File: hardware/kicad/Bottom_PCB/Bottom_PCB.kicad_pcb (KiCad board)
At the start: 4 copper layers, 30.8 x 26.8 mm, 45 parts, among them Q7 IAUC60N04S6N031H, Q8 IAUC60N04S6N031H, Q9 IAUC60N04S6N031H, U5 STSPIN32F0ATR

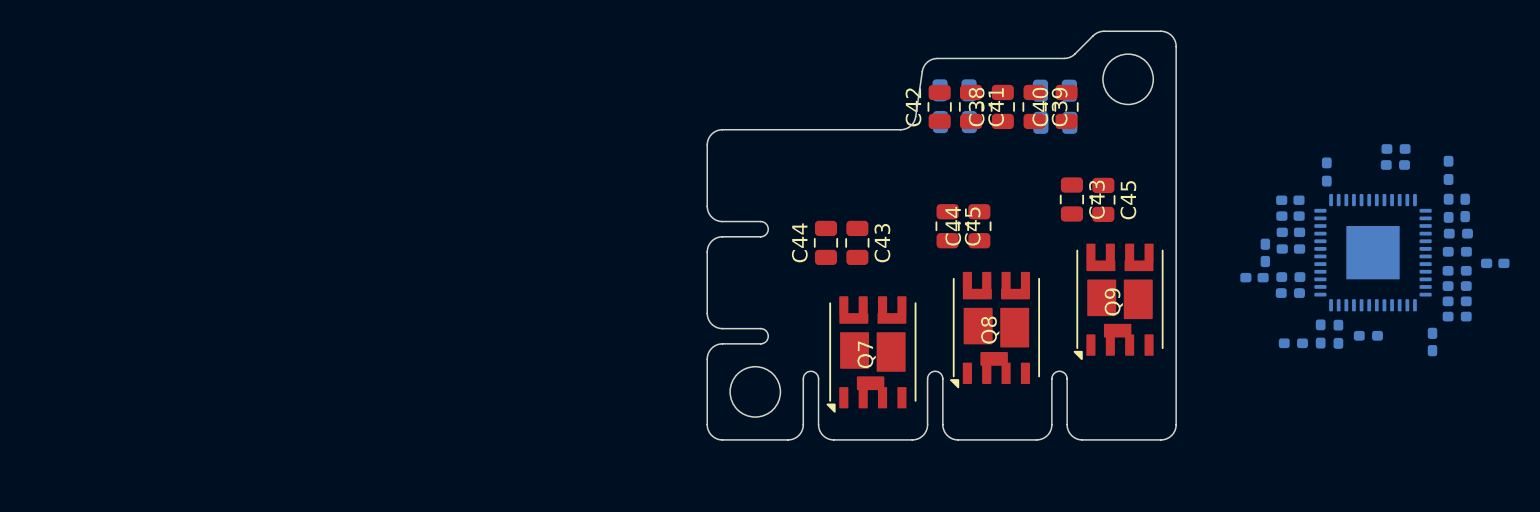
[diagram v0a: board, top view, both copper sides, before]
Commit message: Bottom PCB Design Checked and should be ready for review
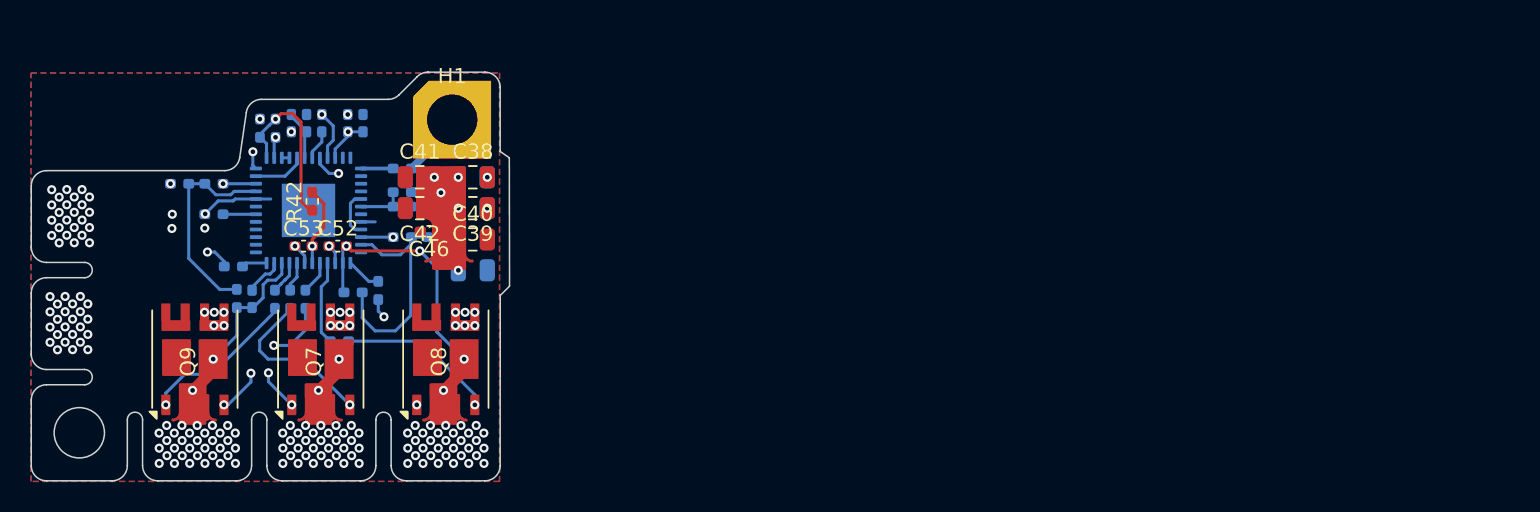
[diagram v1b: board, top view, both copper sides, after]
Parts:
- removed the C39 at (201.8, 88.2)
- removed the C39 at (203.1, 87.1)
- removed the C40 at (203.9, 88.2)
- removed the C40 at (203.1, 89.2)
- removed the C41 at (197.6, 88.2)
- removed the C41 at (196.5, 87.1)
- removed the C42 at (195.5, 88.2)
- removed the C42 at (196.5, 89.2)
- removed the C43 at (204.2, 94.2)
- removed the C43 at (190.1, 97.1)
- removed the C44 at (198.1, 96.0)
- removed the C44 at (188.1, 97.1)
- removed the C45 at (196.1, 96.0)
- removed the C45 at (206.3, 94.3)
- added C39: GRM21BR61A476ME15L, Capacitor_SMD:C_0805_2012Metric, F.Cu at (164.9, 94.8)
- added C40: GRM21BR61A476ME15L, Capacitor_SMD:C_0805_2012Metric, F.Cu at (164.9, 96.8)
- added C41: GRM21BR61A476ME15L, Capacitor_SMD:C_0805_2012Metric, F.Cu at (161.4, 92.8)
- added C42: GRM21BR61A476ME15L, Capacitor_SMD:C_0805_2012Metric, F.Cu at (161.4, 94.8)
- added C43: GRM21BR61A476ME15L, Capacitor_SMD:C_0805_2012Metric, B.Cu at (164.9, 94.8)
- added C44: GRM21BR61A476ME15L, Capacitor_SMD:C_0805_2012Metric, B.Cu at (164.9, 92.8)
- added C45: GRM21BR61A476ME15L, Capacitor_SMD:C_0805_2012Metric, B.Cu at (164.9, 98.9)
- added H1: PWM_Input, MountingHole:MountingHole_2.2mm_M2_DIN965_Pad_TopBottom, F.Cu at (163.6, 89.0)
- added R3: 100k, Resistor_SMD:R_0402_1005Metric_Pad0.72x0.64mm_HandSolder, B.Cu at (160.3, 93.8)
- added R4: 10k, Resistor_SMD:R_0402_1005Metric_Pad0.72x0.64mm_HandSolder, B.Cu at (160.3, 94.7)
- C46, C52, C53, R42: moved to F.Cu
- Q7, Q8, Q9: value IAUC60N04S6N031H -> IAUC60N04S6L045H
- moved R55 80.3 mm to (149.2, 98.6), turned to 180 degrees
- moved C53 78.2 mm to (153.8, 97.3)
- moved R54 77.5 mm to (151.9, 100.8), turned to -90 degrees
- moved C54 77.5 mm to (150.4, 100.8), turned to -90 degrees
- moved R52 76.5 mm to (152.9, 100.8), turned to -90 degrees
- moved R49 76.1 mm to (147.9, 95.2)
- moved R51 75.6 mm to (153.9, 100.8), turned to -90 degrees
- moved R42 75.2 mm to (154.4, 94.3), turned to 90 degrees
- moved C52 74.0 mm to (156.1, 97.3), turned to 0 degrees
- moved R41 73.8 mm to (145.7, 93.2)
- moved R50 73.7 mm to (156.2, 103.5)
- moved R40 73.2 mm to (147.9, 93.2), turned to 180 degrees
- moved R39 72.3 mm to (149.4, 100.7)
- moved R45 72.1 mm to (157.1, 100.3), turned to 0 degrees
- moved R53 70.6 mm to (158.7, 100.2), turned to -90 degrees
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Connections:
- R48 pad 1: /WPWM -> /PWM_INPUT
- U5 pad 18: /VSENSE -> Net-(U5-PA7)
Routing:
- net /BEMF_COMMON: track 0.00 -> 23.9 mm, vias 0 -> 3
- net /PHASE3: track 0.00 -> 16.4 mm, vias 0 -> 37
- net /BEMF3: track 0.00 -> 16.1 mm
- net Net-(Q9-LOW_GATE): track 0.00 -> 15.1 mm, vias 0 -> 3
- net +BATT: track 0.00 -> 13.7 mm, vias 0 -> 30
- net /BEMF1: track 0.00 -> 13.7 mm
- net /PHASE2: track 0.00 -> 13.4 mm, vias 0 -> 36
- net GND: track 0.00 -> 12.2 mm, vias 0 -> 52
- net /BEMF2: track 0.00 -> 11.4 mm, vias 0 -> 1
- net +3.3V: track 0.00 -> 11.0 mm, vias 0 -> 2
- net Net-(Q7-LOW_GATE): track 0.00 -> 11.0 mm, vias 0 -> 1
- net Net-(Q8-LOW_GATE): track 0.00 -> 10.4 mm, vias 0 -> 1
- net Net-(Q9-HIGH_GATE): track 0.00 -> 10.3 mm, vias 0 -> 1
- net /PHASE1: track 0.00 -> 9.10 mm, vias 0 -> 35
- net Net-(Q7-HIGH_GATE): track 0.00 -> 8.59 mm, vias 0 -> 3
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- added copper zone on B.Cu, net GND
- added copper zone on F.Cu, net GND
- added copper zone on In1.Cu, net GND
- added copper zone on In2.Cu, net GND
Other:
- board size 30.8 x 26.8 mm -> 31.4 x 26.8 mm
